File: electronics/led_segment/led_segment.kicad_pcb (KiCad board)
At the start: 2 copper layers, 87.5 x 34.4 mm, 16 parts, among them J1 RJ45, J2 RJ45, J3 Conn_01x04, J4 Screw_Terminal_01x02, J5 Screw_Terminal_01x02, U3 LP2950-5.0_TO252

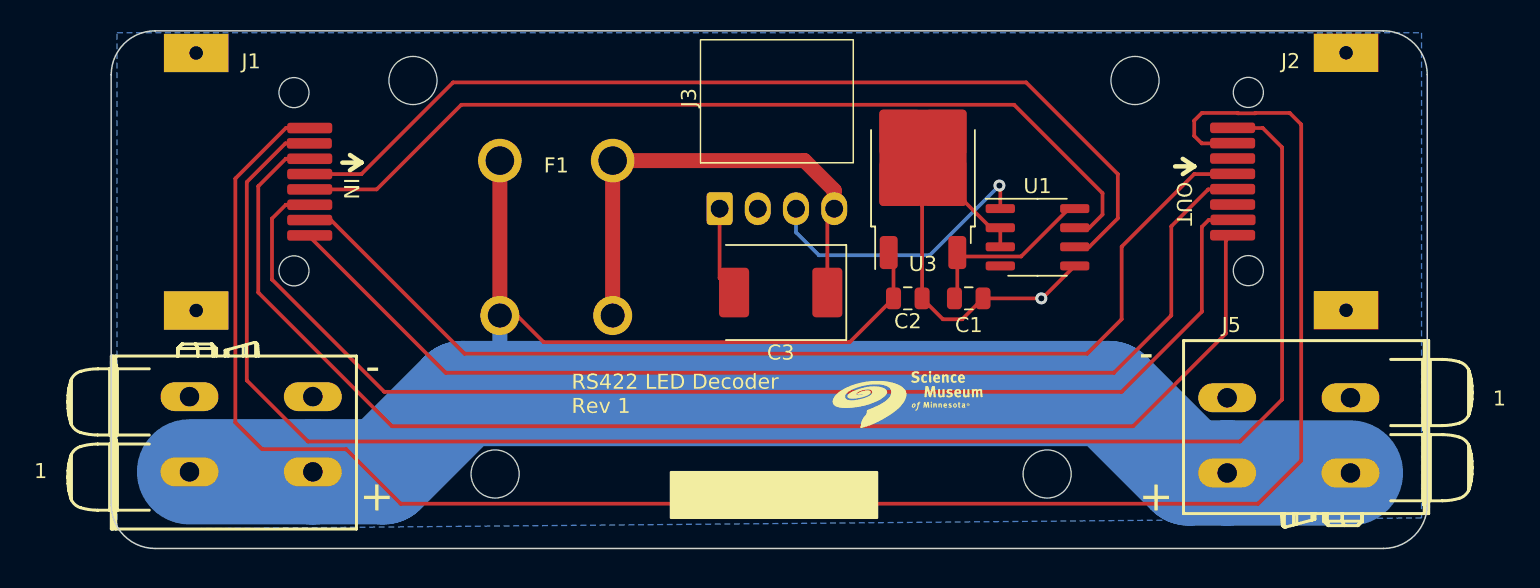
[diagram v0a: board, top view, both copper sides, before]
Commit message: re-implement jumpers
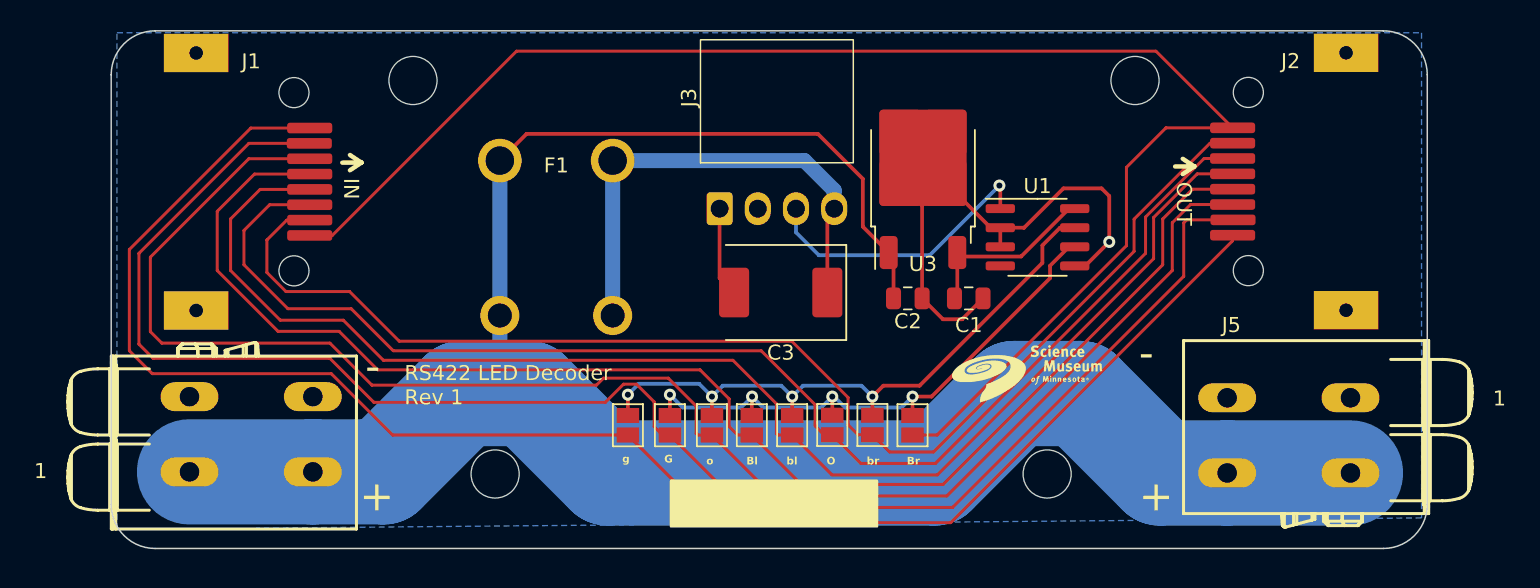
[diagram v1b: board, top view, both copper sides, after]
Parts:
- added JP1: Jumper_2_Open, Jumper:SolderJumper-2_P1.3mm_Open_Pad1.0x1.5mm, F.Cu at (177.0, 146.2)
- added JP2: Jumper_2_Open, Jumper:SolderJumper-2_P1.3mm_Open_Pad1.0x1.5mm, F.Cu at (182.6, 146.2)
- added JP3: Jumper_2_Open, Jumper:SolderJumper-2_P1.3mm_Open_Pad1.0x1.5mm, F.Cu at (188.0, 146.2)
- added JP4: Jumper_2_Open, Jumper:SolderJumper-2_P1.3mm_Open_Pad1.0x1.5mm, F.Cu at (193.3, 146.2)
- added JP5: Jumper_2_Open, Jumper:SolderJumper-2_P1.3mm_Open_Pad1.0x1.5mm, F.Cu at (179.8, 146.2)
- added JP6: Jumper_2_Open, Jumper:SolderJumper-2_P1.3mm_Open_Pad1.0x1.5mm, F.Cu at (190.6, 146.2)
- added JP7: Jumper_2_Open, Jumper:SolderJumper-2_P1.3mm_Open_Pad1.0x1.5mm, F.Cu at (185.3, 146.2)
- added JP8: Jumper_2_Open, Jumper:SolderJumper-2_P1.3mm_Open_Pad1.0x1.5mm, F.Cu at (196.0, 146.2)
- moved G*** 8.12 mm to (203.6, 142.7)
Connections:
- J2 pad 1: /O- -> /G-
- J2 pad 2: /O+ -> /G+
- J2 pad 3: unconnected-(J2-Pad3) -> /O-
- J2 pad 4: /Br+ -> /Bl+
- J2 pad 5: /Br- -> /Bl-
- J2 pad 6: unconnected-(J2-Pad6) -> /O+
- J2 pad 7: /G- -> /Br-
- J2 pad 8: /G+ -> /Br+
- U1 pad 6: /Bl+ -> Net-(JP5-B)
- U1 pad 7: /Bl- -> Net-(JP1-B)
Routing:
- net Net-(JP1-B): track 0.00 -> 42.3 mm, vias 0 -> 4
- net Net-(JP5-B): track 0.00 -> 38.9 mm, vias 0 -> 4
- net /Bl-: track 61.2 -> 92.8 mm
- net /Bl+: track 65.5 -> 95.5 mm
- net /Br+: track 73.6 -> 101.3 mm
- net /G-: track 130.4 -> 108.3 mm
- net /O-: track 88.4 -> 106.1 mm
- net /Br-: track 72.8 -> 85.5 mm
- net +12V: track 128.5 -> 137.3 mm
- net GND: track 32.6 -> 40.1 mm
- net /O+: track 81.8 -> 89.2 mm
- net /G+: track 110.7 -> 109.6 mm
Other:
- board text added: "Bl"
- board text added: "Br"
- board text added: "G"
- board text added: "O"
- board text added: "bl"
- board text added: "br"
- board text added: "g"
- board text added: "o"

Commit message: get peer review on rev.3 of boards
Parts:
- removed the REF** at (204.9, 149.4)
- removed the REF** at (210.8, 123.3)
- removed the REF** at (168.2, 149.4)
- removed the REF** at (162.7, 123.3)
- added D1: LED, LED_THT:LED_D3.0mm, F.Cu at (193.5, 122.6)
- added JP9: Jumper_2_Open, Jumper:SolderJumper-2_P1.3mm_Open_Pad1.0x1.5mm, F.Cu at (179.9, 126.9)
- added R1: R, Resistor_SMD:R_1206_3216Metric, F.Cu at (204.5, 138.0)
- added R2: R, Resistor_SMD:R_1206_3216Metric, F.Cu at (202.5, 128.1)
- added REF**: MountingHole_3.2mm_M3, MountingHole:MountingHole_3.2mm_M3, F.Cu at (204.1, 123.3)
- added REF**: MountingHole_3.2mm_M3, MountingHole:MountingHole_3.2mm_M3, F.Cu at (168.1, 150.3)
- added REF**: MountingHole_3.2mm_M3, MountingHole:MountingHole_3.2mm_M3, F.Cu at (205.0, 150.3)
- J1, J2: footprint SMM:RC01516 -> Connector_RJ:RJ45_Ninigi_GE
- moved G*** 36.3 mm to (167.3, 142.3)
- moved J1 7.72 mm to (158.3, 125.3)
- moved J2 7.65 mm to (214.6, 134.3)
- moved JP1 4.86 mm to (177.7, 151.0), turned to -90 degrees
- moved JP2 4.86 mm to (183.3, 151.0), turned to -90 degrees
- moved JP3 4.86 mm to (188.6, 151.0), turned to -90 degrees
- moved JP5 4.86 mm to (180.5, 151.0), turned to -90 degrees
- moved JP7 4.86 mm to (185.9, 151.0), turned to -90 degrees
- moved JP8 4.86 mm to (196.6, 151.0), turned to -90 degrees
- moved JP4 4.86 mm to (194.0, 151.0), turned to -90 degrees
- moved JP6 4.86 mm to (191.3, 151.0), turned to -90 degrees
- moved C3 1.21 mm to (187.0, 138.6)
- moved J3 0.53 mm to (183.2, 131.2)
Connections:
- J3 pad 2: GND -> Net-(J3-Pin_2)
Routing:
- net GND: track 40.1 -> 139.8 mm
- net Net-(JP5-B): track 38.9 -> 89.1 mm, vias 4 -> 2
- net +12V: track 137.3 -> 98.0 mm
- net Net-(JP1-B): track 42.3 -> 79.5 mm, vias 4 -> 2
- net /Br-: track 85.5 -> 120.5 mm, vias 0 -> 1
- net /O+: track 89.2 -> 113.7 mm, vias 0 -> 1
- net /G+: track 109.6 -> 85.6 mm, vias 0 -> 1
- net /G-: track 108.3 -> 86.4 mm, vias 0 -> 1
- net /Br+: track 101.3 -> 120.9 mm, vias 0 -> 1
- net Net-(J3-Pin_3): track 19.2 -> 29.9 mm
- net /Bl-: track 92.8 -> 103.4 mm, vias 0 -> 1
- net /Bl+: track 95.5 -> 106.1 mm, vias 0 -> 1
- net Net-(D1-A): track 0.00 -> 9.46 mm
- net Net-(J3-Pin_4): track 32.8 -> 42.1 mm
- net Net-(J3-Pin_2): track 0.00 -> 7.34 mm
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- added copper zone on F.Cu, net +12V
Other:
- copper layers 2 -> 4
- board text added: "330_CSS RS422 LED Decoder Rev 3"
- board text removed: "RS422 LED Decoder Rev 1"
